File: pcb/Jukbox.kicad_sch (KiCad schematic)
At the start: 3 parts, among them J1 Raspberry_Pi_2_3, U2 MAX98357A

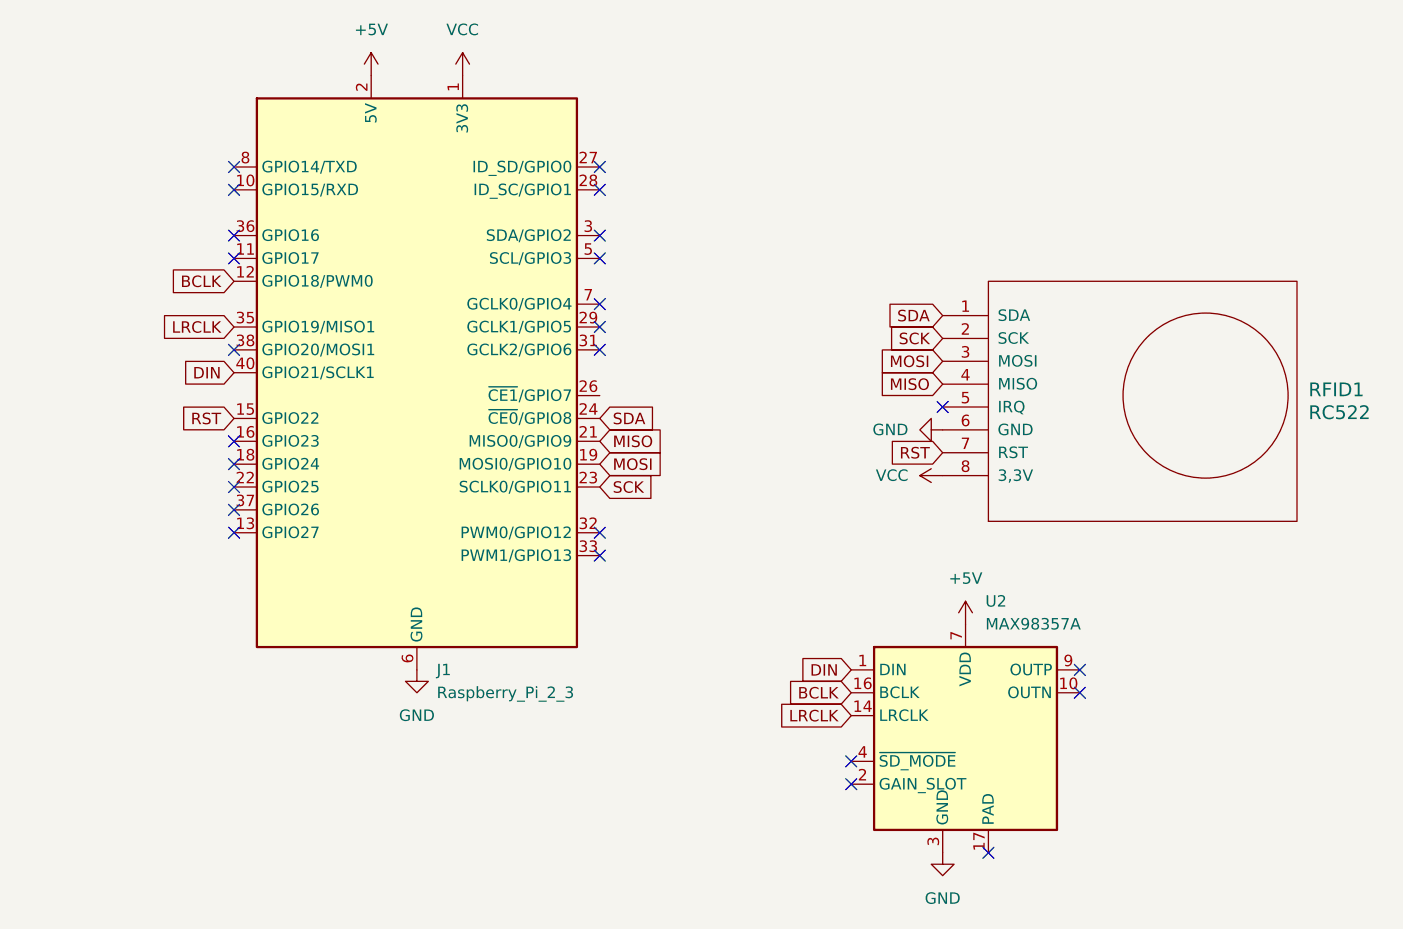
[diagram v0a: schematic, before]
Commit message: added buttons
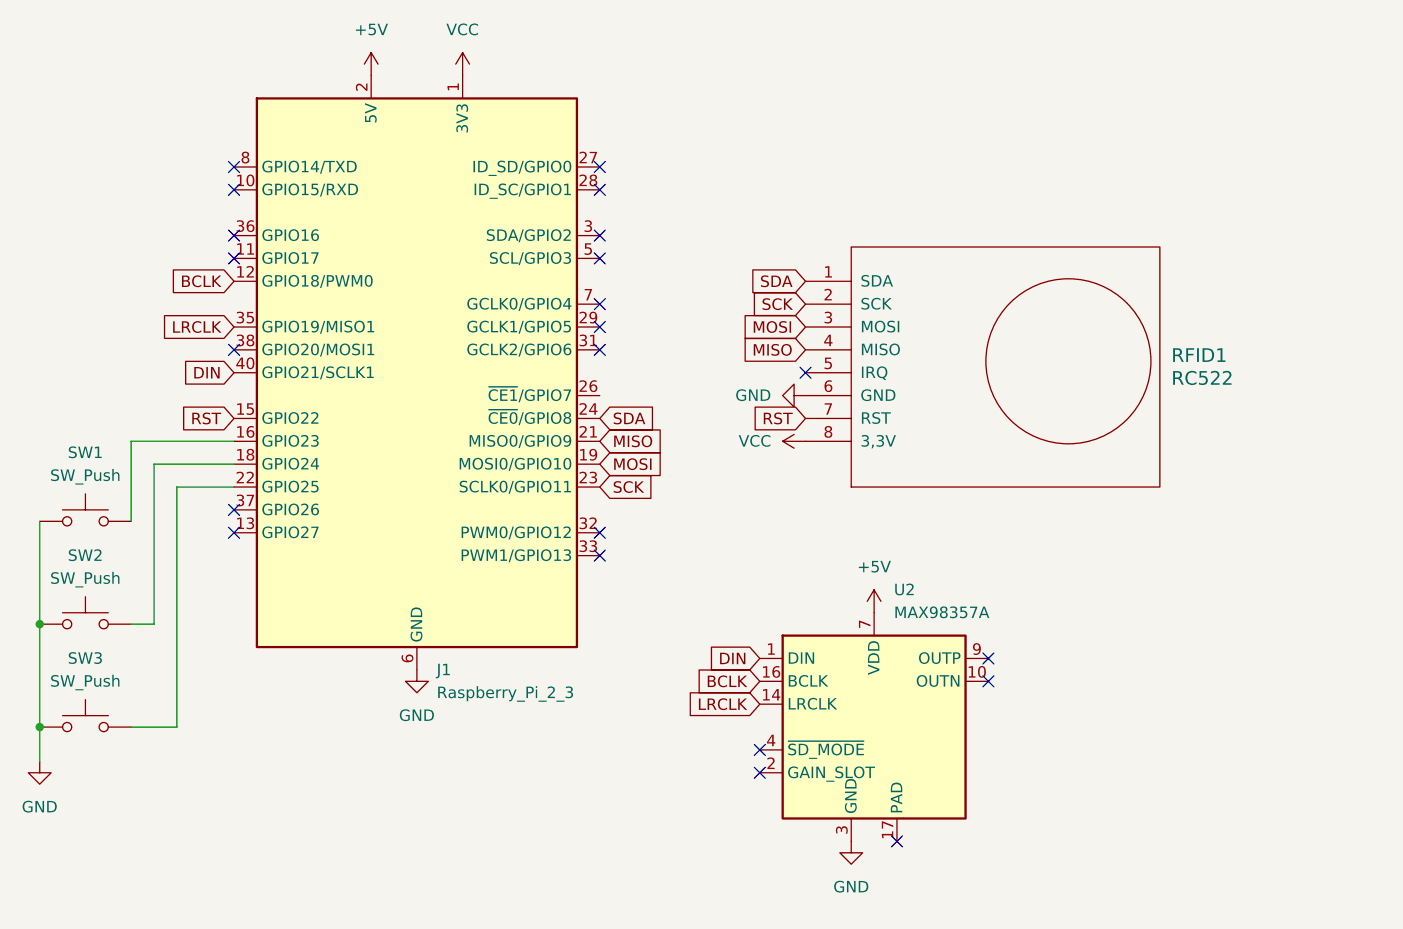
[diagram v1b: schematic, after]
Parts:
- added SW1, SW2, SW3: SW_Push, Button_Switch_Keyboard:SW_Cherry_MX_1.00u_PCB, symbol Switch:SW_Push
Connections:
- net GND: now also SW1.1, SW2.1, SW3.1
- net at J1.16 (GPIO23): now also SW1.2
- net at J1.18 (GPIO24): now also SW2.2
- net at J1.22 (GPIO25): now also SW3.2
- no-connect marks 25 -> 22
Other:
- moved on the sheet: RFID1, U2
